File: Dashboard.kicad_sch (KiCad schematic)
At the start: 0 parts

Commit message: Filled in Many Sheets
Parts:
- added D? (x2): LED, symbol Simulation_SPICE:DIODE
- added F?: 1A Fuse, symbol Device:Fuse
- added U?: Start Button, symbol SCR23 Library:Pushbutton_(Open)
- added U?: E_Stop, symbol SCR23 Library:Switch
- added U?: Ignition Switch, symbol SCR23 Library:Switch
- added U?: Brake Over-travel, symbol SCR23 Library:Switch
- added U?: Shift Down, symbol SCR23 Library:Pushbutton_(Open)
- added U?: DTM_Dash, symbol SCR23 Library:DTM_Dash
- added U?: Shift Up, symbol SCR23 Library:Pushbutton_(Open)
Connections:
- new net: D?.1 (A), U?., U?.
- new net: U?., U?.
- new net: F?.2, U?., U?.
- new net Fuse 1 Power: U?.
- new net GND: D?.2 (K)
- new net IGN Signal: D?.1 (A), U?., U?.
- new net Starter Relay Control: U?.

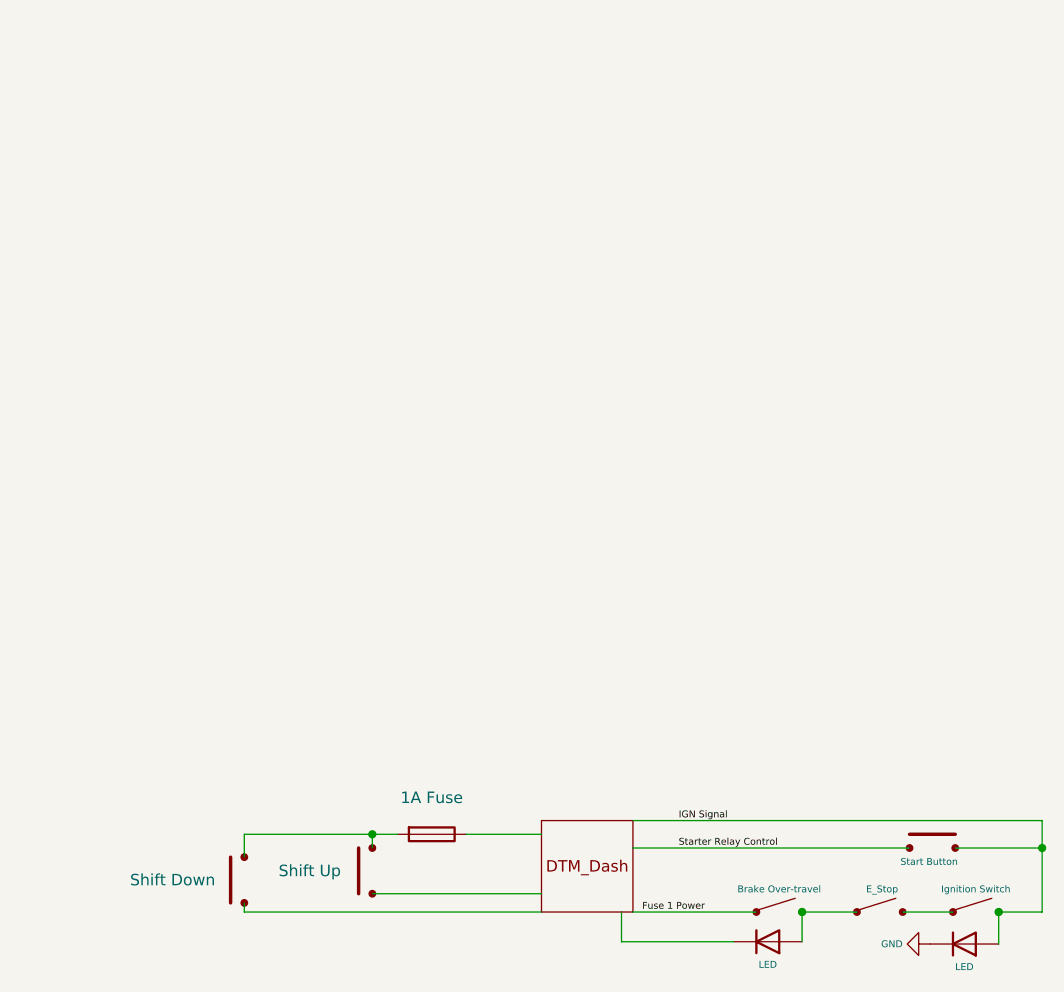
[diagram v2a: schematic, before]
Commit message: Change to coil driver
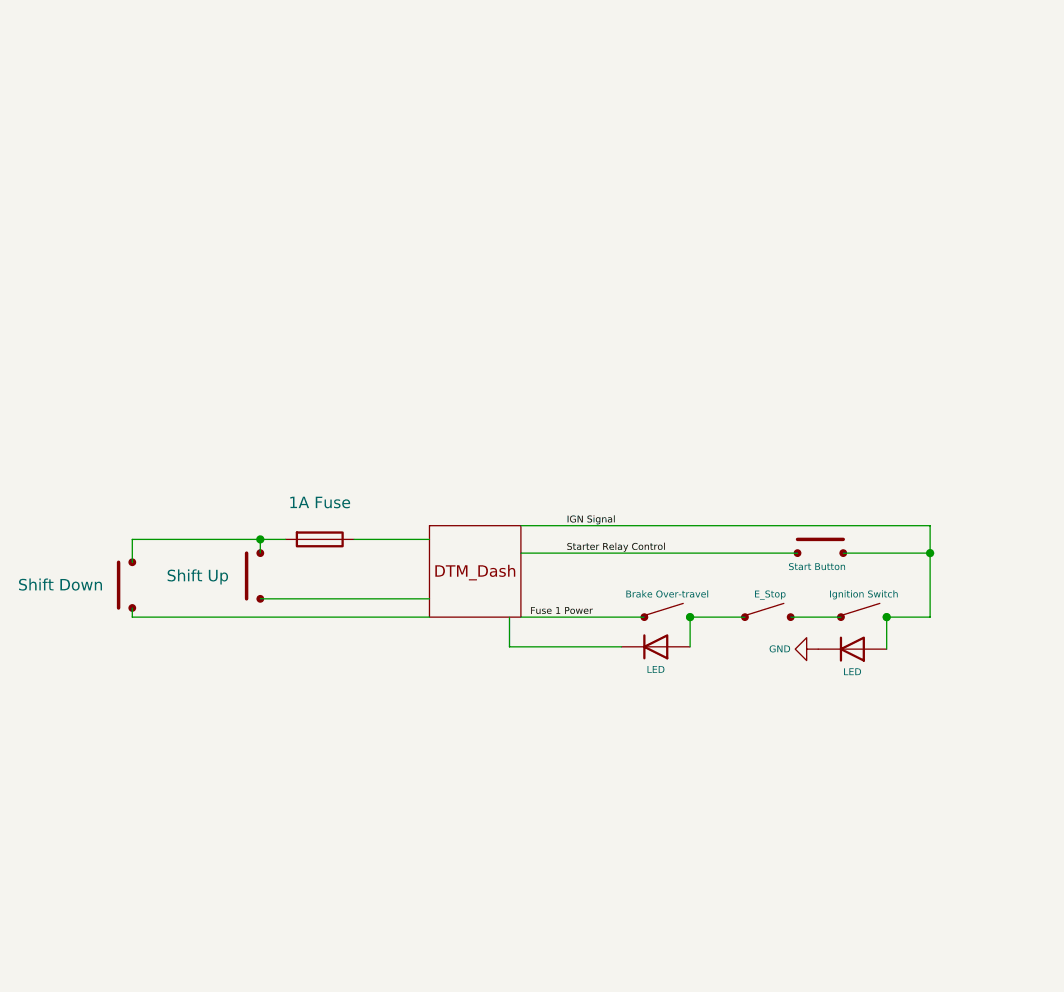
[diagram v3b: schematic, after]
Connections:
- new net: D?.1 (A), U?., U?.
- new net: F?.2, U?., U?.
- now unconnected: U?., U?.

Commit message: Infinity 5 and 7 Pinouts
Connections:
- new net: D?.1 (A), U?., U?.
- new net: F?.2, U?., U?.
- now unconnected: U?., U?.

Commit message: Dash and Engine Update
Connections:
- new net: D?.1 (A), U?., U?.
- new net: F?.2, U?., U?.
- now unconnected: U?., U?.

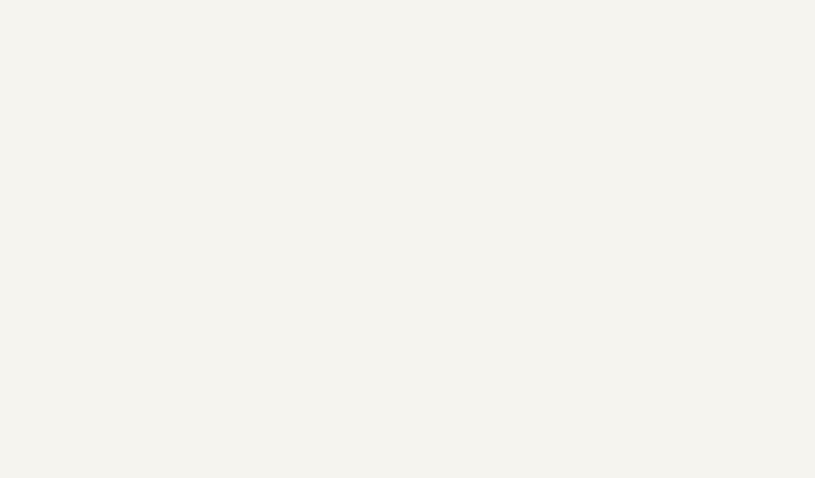
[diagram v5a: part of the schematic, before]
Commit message: Updated Connectors
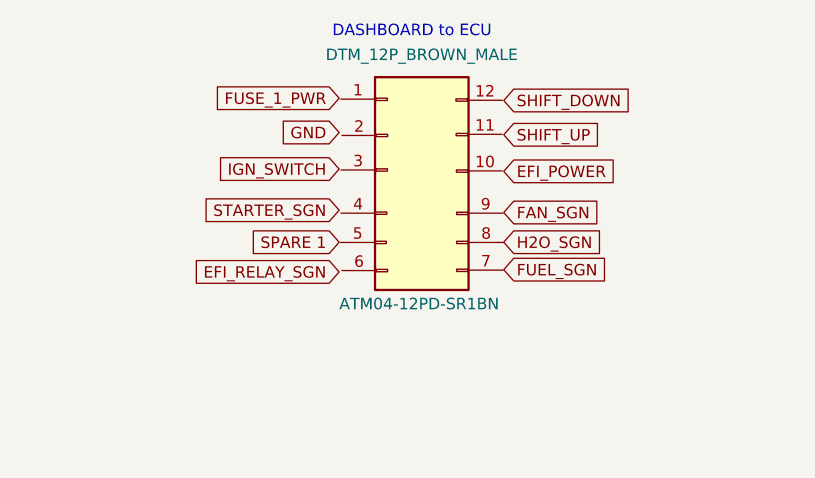
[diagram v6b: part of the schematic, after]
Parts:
- added U?: DTM_12P_BROWN_MALE, symbol SCR23 Library:DTM04-12pb
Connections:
- new net: D?.1 (A), U?., U?.
- new net: F?.2, U?., U?.
- now unconnected: U?., U?.
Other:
- note added: "DASHBOARD to ECU"
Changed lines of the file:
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@@
     (stroke (width 0) (type default) (color 0 0 0 0))
+  )
+  (text "DASHBOARD to ECU" (at 131.064 41.148 0)
+    (effects (font (size 1.27 1.27)) (justify left bottom))
   )
   (label "Starter Relay Control" (at 149.606 98.298 0)
@@
   (label "IGN Signal" (at 149.606 95.25 0)
     (effects (font (size 0.762 0.762)) (justify left bottom))
+  )
+  (global_label "EFI_RELAY_SGN" (shape input) (at 131.826 67.056 180) (fields_autoplaced)
+    (effects (font (size 1.27 1.27)) (justify right))
+    (property "Intersheet References" "${INTERSHEET_REFS}" (id 0) (at 115.201 66.9766 0)
+      (effects (font (size 1.27 1.27)) (justify right) hide)
+    )
+  )
+  (global_label "EFI_POWER" (shape input) (at 150.114 55.88 0) (fields_autoplaced)
+    (effects (font (size 1.27 1.27)) (justify left))
+    (property "Intersheet References" "${INTERSHEET_REFS}" (id 0) (at 162.8081 55.8006 0)
+      (effects (font (size 1.27 1.27)) (justify left) hide)
+    )
+  )
+  (global_label "SHIFT_DOWN" (shape input) (at 150.114 48.006 0) (fields_autoplaced)
+    (effects (font (size 1.27 1.27)) (justify left))
+    (property "Intersheet References" "${INTERSHEET_REFS}" (id 0) (at 164.0781 47.9266 0)
+      (effects (font (size 1.27 1.27)) (justify left) hide)
+    )
+  )
+  (global_label "SHIFT_UP" (shape input) (at 150.114 51.816 0) (fields_autoplaced)
+    (effects (font (size 1.27 1.27)) (justify left))
+    (property "Intersheet References" "${INTERSHEET_REFS}" (id 0) (at 161.2961 51.7366 0)
+      (effects (font (size 1.27 1.27)) (justify left) hide)
+    )
+  )
+  (global_label "IGN_SWITCH" (shape input) (at 131.826 55.626 180) (fields_autoplaced)
+    (effects (font (size 1.27 1.27)) (justify right))
+    (property "Intersheet References" "${INTERSHEET_REFS}" (id 0) (at 118.4062 55.5466 0)
+      (effects (font (size 1.27 1.27)) (justify right) hide)
+    )
+  )
+  (global_label "FAN_SGN" (shape input) (at 150.114 60.452 0) (fields_autoplaced)
+    (effects (font (size 1.27 1.27)) (justify left))
+    (property "Intersheet References" "${INTERSHEET_REFS}" (id 0) (at 160.8123 60.3726 0)
+      (effects (font (size 1.27 1.27)) (justify left) hide)
+    )
+  )
+  (global_label "SPARE 1" (shape input) (at 131.826 63.754 180) (fields_autoplaced)
+    (effects (font (size 1.27 1.27)) (justify right))
+    (property "Intersheet References" "${INTERSHEET_REFS}" (id 0) (at 121.2486 63.6746 0)
+      (effects (font (size 1.27 1.27)) (justify right) hide)
+    )
+  )
+  (global_label "H2O_SGN" (shape input) (at 150.114 63.754 0) (fields_autoplaced)
+    (effects (font (size 1.27 1.27)) (justify left))
+    (property "Intersheet References" "${INTERSHEET_REFS}" (id 0) (at 161.1752 63.6746 0)
+      (effects (font (size 1.27 1.27)) (justify left) hide)
+    )
+  )
+  (global_label "FUSE_1_PWR" (shape input) (at 131.826 47.752 180) (fields_autoplaced)
+    (effects (font (size 1.27 1.27)) (justify right))
+    (property "Intersheet References" "${INTERSHEET_REFS}" (id 0) (at 117.4991 47.6726 0)
+      (effects (font (size 1.27 1.27)) (justify right) hide)
+    )
+  )
+  (global_label "STARTER_SGN" (shape input) (at 131.826 60.198 180) (fields_autoplaced)
+    (effects (font (size 1.27 1.27)) (justify right))
+    (property "Intersheet References" "${INTERSHEET_REFS}" (id 0) (at 116.7129 60.1186 0)
+      (effects (font (size 1.27 1.27)) (justify right) hide)
+    )
+  )
+  (global_label "FUEL_SGN" (shape input) (at 150.114 66.802 0) (fields_autoplaced)
+    (effects (font (size 1.27 1.27)) (justify left))
+    (property "Intersheet References" "${INTERSHEET_REFS}" (id 0) (at 161.9009 66.7226 0)
+      (effects (font (size 1.27 1.27)) (justify left) hide)
+    )
+  )
+  (global_label "GND" (shape input) (at 131.826 51.562 180) (fields_autoplaced)
+    (effects (font (size 1.27 1.27)) (justify right))
+    (property "Intersheet References" "${INTERSHEET_REFS}" (id 0) (at 125.5424 51.4826 0)
+      (effects (font (size 1.27 1.27)) (justify right) hide)
+    )
   )
   (symbol (lib_id "Simulation_SPICE:DIODE") (at 181.356 108.966 0) (mirror y) (unit 1)
@@
     (pin "2")
   )
+  (symbol (lib_id "SCR23 Library:DTM04-12pb") (at 140.716 58.166 0) (unit 1)
+    (in_bom yes) (on_board yes)
+    (property "Reference" "U?" (id 0) (at 141.0081 40.386 0)
+      (effects (font (size 1.27 1.27)) hide)
+    )
+    (property "Value" "DTM_12P_BROWN_MALE" (id 1) (at 141.0081 42.926 0))
+    (property "Footprint" "" (id 2) (at 140.716 68.326 0)
+      (effects (font (size 1.27 1.27)) hide)
+    )
+    (property "Datasheet" "" (id 3) (at 140.716 68.326 0)
+      (effects (font (size 1.27 1.27)) hide)
+    )
+    (property "Part #" "ATM04-12PD-SR1BN" (id 4) (at 140.716 70.612 0))
+    (pin "1")
+    (pin "10")
+    (pin "11")
+    (pin "12")
+    (pin "2")
+    (pin "3")
+    (pin "4")
+    (pin "5")
+    (pin "6")
+    (pin "7")
+    (pin "8")
+    (pin "9")
+  )
   (symbol (lib_id "SCR23 Library:Switch") (at 160.782 105.41 0) (unit 1)

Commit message: Updated Connectors
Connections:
- new net: D?.1 (A), U?., U?.
- new net: F?.2, U?., U?.
- now unconnected: U?., U?.
